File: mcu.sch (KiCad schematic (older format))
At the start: 29 parts, among them IC2 LM4040CYM3-2.5, P1 CONN_01X02, SW1 SW_PUSH, SW2 Rotary_Switch, T2 MMBT3904, U2 STM32F072CB, Y1 8kHz, Y2 ABS25-32.768KHZ-6-T

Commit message: Updated R/C/L symbols to IEC 60617 style
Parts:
- D6: renamed from IC2; symbol TEXAS_LM4041A12DBZ -> LM4040
- LED1, LED2: symbol LED-RESCUE-MPPT_Charger_20A -> LED
- renumbered SW2 to S1
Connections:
- wire segments 118 -> 116
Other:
- note added: "min. 65 uA\noperating\ncurrent"
- note removed: "L4: Murata\nBLM18AG601SN1D"
- note removed: "min. 65 uA operating\ncurrent needed"
- moved on the sheet: C27, C28, C29, C30, C31, C32, C33, C34, C36, L4, P1, R30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

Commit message: Updated revision: 0.8
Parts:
- removed C27, C28: 4.3p, Capacitors_SMD:C_0603, symbol C
- removed R30: 0, Resistors_SMD:R_0603, symbol R
- removed S1: Rotary_Switch, LibreSolar:Rotary_Switch_THT, symbol Rotary_Switch
- removed Y2: ABS25-32.768KHZ-6-T, Crystals:Crystal_SMD_SeikoEpson_MC306-4pin_8.0x3.2mm, symbol Crystal_NC23
- added C22: 100n, LibreSolar:C_0603_1608, symbol C
- added LED3, LED4: LED, LEDs:LED_0603, symbol LED
- added R31, R32: 2.2k, LibreSolar:R_0603_1608, symbol R
- added U6: 24AA01, TO_SOT_Packages_SMD:SOT-23-5, symbol 24AA01
- C29, C30, C31, C32, C34: footprint Capacitors_SMD:C_0603 -> LibreSolar:C_0603_1608; MFR Murata -> (none); MPN GRM188R71H104KA93D -> (none); Manufacturer (none) -> Murata; PartNumber (none) -> GRM188R71H104KA93D
- C33, C36: footprint Capacitors_SMD:C_0603 -> LibreSolar:C_0603_1608; MFR Murata -> (none); MPN GRM188R60J225KE19D -> (none); Manufacturer (none) -> Murata; PartNumber (none) -> GRM188R60J225KE19D
- D6: footprint TO_SOT_Packages_SMD:SOT-23 -> LibreSolar:SOT-23; MFR Microchip -> (none); MPN LM4040DYM3-2.5-TR -> (none); Manufacturer (none) -> Microchip; PartNumber (none) -> LM4040DYM3-2.5-TR
- L4: value L -> 600R; MFR Murata -> (none); MPN BLM18AG601SN1D -> (none); Manufacturer (none) -> Murata; PartNumber (none) -> BLM18AG601SN1D
- R37: footprint Resistors_SMD:R_0603 -> LibreSolar:R_0603_1608; MFR Yageo -> (none); MPN RC0603FR-07150KL -> (none); Manufacturer (none) -> Yageo; PartNumber (none) -> RC0603FR-07150KL
- R39, R40: footprint Resistors_SMD:R_0603 -> LibreSolar:R_0603_1608; MFR Yageo -> (none); MPN RC0603FR-071ML -> (none); Manufacturer (none) -> Yageo; PartNumber (none) -> RC0603FR-071ML
- R41: footprint Resistors_SMD:R_0603 -> LibreSolar:R_0603_1608; MFR Yageo -> (none); MPN RC0603FR-072K2L -> (none); Manufacturer (none) -> Yageo; PartNumber (none) -> RC0603FR-072K2L
- R42, R43: footprint Resistors_SMD:R_0603 -> LibreSolar:R_0603_1608; MFR Yageo -> (none); MPN RC0603FR-07330RL -> (none); Manufacturer (none) -> Yageo; PartNumber (none) -> RC0603FR-07330RL
- R45: footprint Resistors_SMD:R_0603 -> LibreSolar:R_0603_1608; MFR Yageo -> (none); MPN RC0603FR-0756KL -> (none); Manufacturer (none) -> Yageo; PartNumber (none) -> RC0603FR-0756KL
- SW1: footprint Buttons_Switches_THT:SW_PUSH_6mm -> LibreSolar:SW_SPST_EVQP7A; Manufacturer (none) -> C&K Components; PartNumber (none) -> PTS840 GK SMTR LFS
- T2: footprint TO_SOT_Packages_SMD:SOT-23 -> LibreSolar:SOT-23; MFR Diodes Inc. -> (none); MPN MMBT3904-7-F -> (none); Manufacturer (none) -> Diodes Inc.; PartNumber (none) -> MMBT3904-7-F
- U2: MFR STMicroelectronics -> (none); MPN STM32F072CB -> (none); Manufacturer (none) -> STMicroelectronics; PartNumber (none) -> STM32F072CBT6
- Y1: symbol CRYSTAL_SMD -> Resonator; MFR Murata -> (none); MPN CSTCE8M00G15C99-R0 -> (none); Manufacturer (none) -> Murata; PartNumber (none) -> CSTCE8M00G15C99-R0; Tolerance (none) -> 0.1%
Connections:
- net +3V3: now also C22.1, R31.2, R32.2, U6.4 (VCC)
- net GND: now also C22.2, LED3.1 (K), LED4.1 (K), U6.2 (GND), U6.5 (WP)
- net at LED1.2 (A), R42.1: now also LED3.2 (A)
- net at LED2.2 (A), R43.1: now also LED4.2 (A)
- net REF_I_DCDC renamed DAC
- net ROT_0 renamed I2C2_SCL
- net I2C2_SCL: now also R31.1, U6.1 (SCL)
- net ROT_1 renamed I2C2_SDA
- net I2C2_SDA: now also R32.1, U6.3 (SDA)
- net ROT_2 renamed 5V_OUT_EN
- no-connect marks 4 -> 3
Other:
- note added: "EEPROM"
- note added: "Equations:\ntau = R39 * C36 = 2.2 s\nV(t) = Vmax * (1-exp(-t/tau))\n--> t = -tau * ln(1-V/Vmax)\n\nNormal startup:\nBOOT0 < 0.69 V\nPress SW1 < 0.51 s\n\nUSB bootloader:\nBOOT0 > 1.61 V\nPress SW1 > 1.47 s"
- note added: "Tight tolerance\nfor CAN interface"
- note removed: "Mode switch"
- note removed: "Reset & boot switch\n- Press long (>2s) for USB bootloader\n (BOOT0 cap charged)\n- Press short (<1s) for normal reset"
- note removed: "Should be 0.1% tolerance\nfor CAN interface, e.g.\nCSTCE8M00G15C99-R0"
- moved on the sheet: C29, C30, C31, C32, C33, C36, D6, LED1, LED2, R37, R39, R40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

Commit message: Minor changes and gerber export update
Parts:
- C33, C36: Remarks (none) -> 6.3V, X5R
- Y1: Remarks (none) -> 0.1% tolerance; Tolerance 0.1% -> (none)
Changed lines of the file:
@@
 F 7 "" H 3600 -700 50  0001 C CNN "SPN"
 F 8 "" H 3600 -700 50  0001 C CNN "SPURL"
+F 9 "" H 0   0   60  0001 C CNN "Comment"
+F 10 "6.3V, X5R" H 0   0   60  0001 C CNN "Remarks"
 	1    6050 4800
 	1    0    0    -1
@@
 F 7 "" H -250 0   50  0001 C CNN "SPN"
 F 8 "" H -250 0   50  0001 C CNN "SPURL"
+F 9 "" H 0   0   60  0001 C CNN "Comment"
+F 10 "6.3V, X5R" H 0   0   60  0001 C CNN "Remarks"
 	1    9100 2700
 	1    0    0    -1
@@
 F 4 "Murata" H 0   -2950 50  0001 C CNN "Manufacturer"
 F 5 "CSTCE8M00G15C99-R0" H 0   -2950 50  0001 C CNN "PartNumber"
-F 6 "0.1%" H 5150 1150 50  0000 L CNN "Tolerance"
+F 6 "" H 5150 1150 50  0000 L CNN "Tolerance"
+F 7 "0.1% tolerance" H 0   0   60  0001 C CNN "Remarks"
 	1    5100 1400
 	1    0    0    -1

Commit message: V0.8.1: Small changes and update to new kicad symbol library table (nightlies only)
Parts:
- removed LED3, LED4: LED, LEDs:LED_0603, symbol LED
- C22, C29, C30, C31, C32, C33, C34, C36: symbol C -> device:C_Small
- D6: symbol LM4040 -> device:D_Zener_Small
- L4: symbol L -> device:L_Small
- LED1: footprint LEDs:LED_D3.0mm -> LEDs:LED_0603; symbol LED -> device:LED_Small; Manufacturer (none) -> Lite-On; PartNumber (none) -> LTST-C190KRKT; Remarks (none) -> red
- LED2: footprint LEDs:LED_D3.0mm -> LEDs:LED_0603; symbol LED -> device:LED_Small; Manufacturer (none) -> Lite-On; PartNumber (none) -> LTST-C190GKT
- P1: symbol CONN_01X02 -> Connector:Conn_01x02
- R31, R32, R37, R39, R40, R41, R42, R43, R45: symbol R -> device:R_Small
- SW1: symbol SW_PUSH -> IEC-60617:SW_PUSH
- SWD1: symbol ST_Nucleo_SWD -> LibreSolar:ST_Nucleo_SWD
- T2: symbol MMBT3904 -> Transistor:BC817
- U2: symbol STM32F072CB -> LibreSolar:STM32F072CB
- U6: symbol 24AA01 -> LibreSolar:24AA01; PartNumber 24AA01 -> 24AA32AFT-I/OT
- Y1: value 8kHz -> 8MHz; footprint LibreSolar:Resonator_Murata_CSTCE -> LibreSolar:Resonator_Murata_CSTCE_G; symbol Resonator -> device:Resonator_Small; Tolerance (none) -> 0.1%
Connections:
- net GND: now also Y1.2; no longer Y1.3
- net OSC_OUT: now also Y1.3; no longer Y1.2
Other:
- moved on the sheet: LED1, LED2, R42, R43

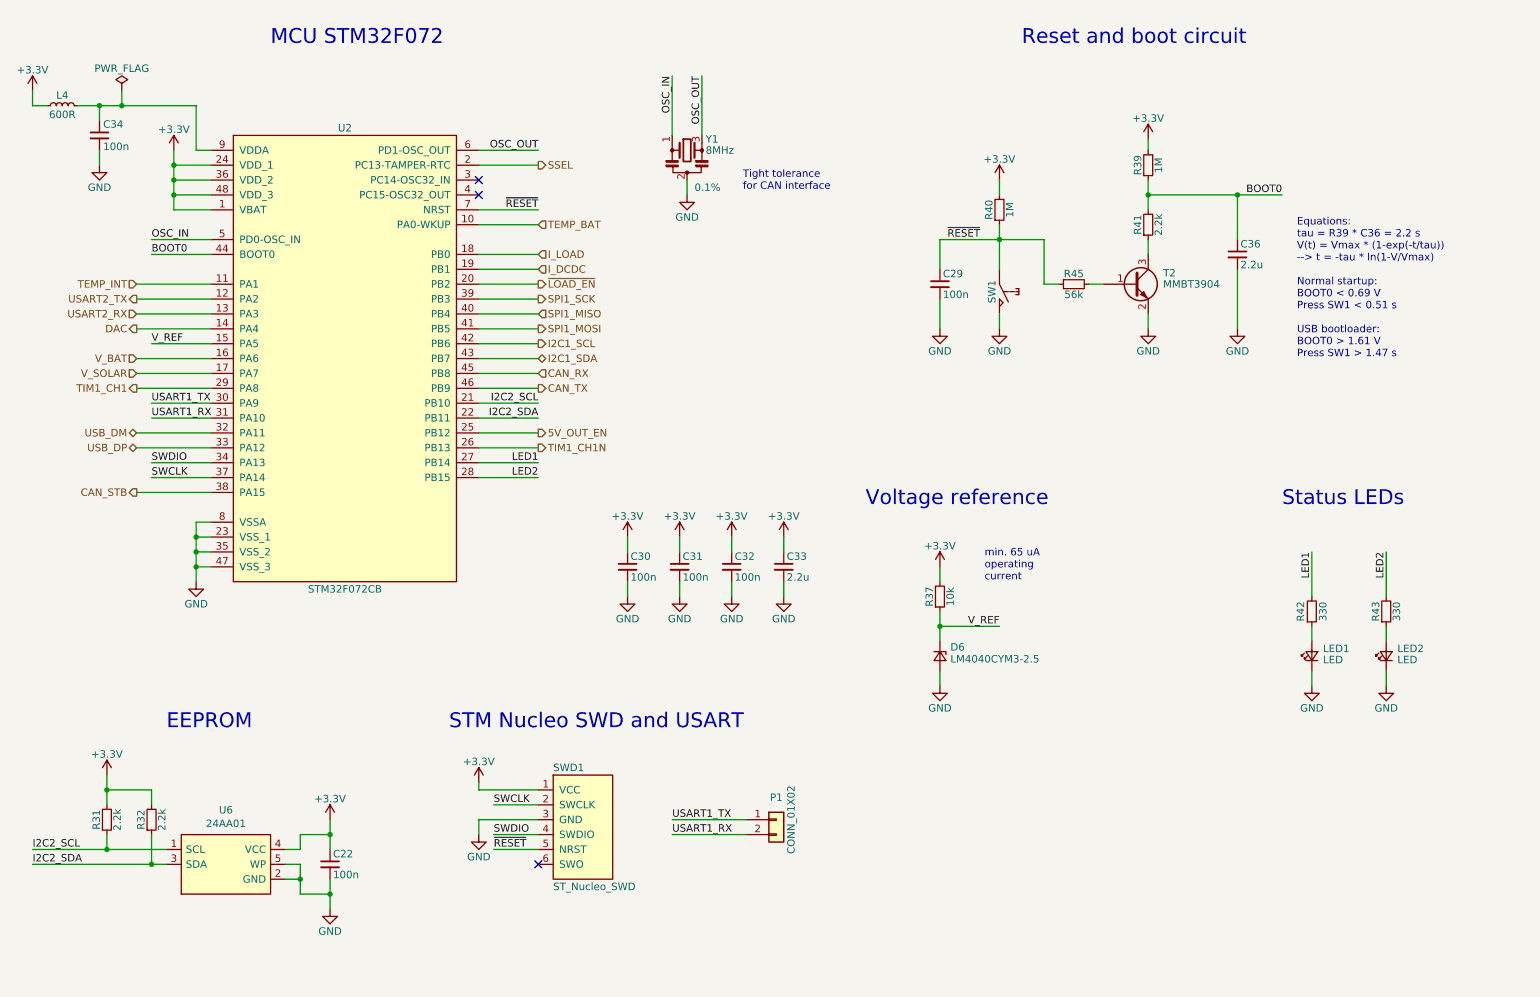
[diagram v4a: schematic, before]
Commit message: Revision 0.9 for first small production batch - Switchable power supply for bus and UEXT (to be make sure to reach very low power consumption during LVD conditions) - MLCCs for EMC added to each high power input/output - Re-arrangement of some connectors after initial tests with housing
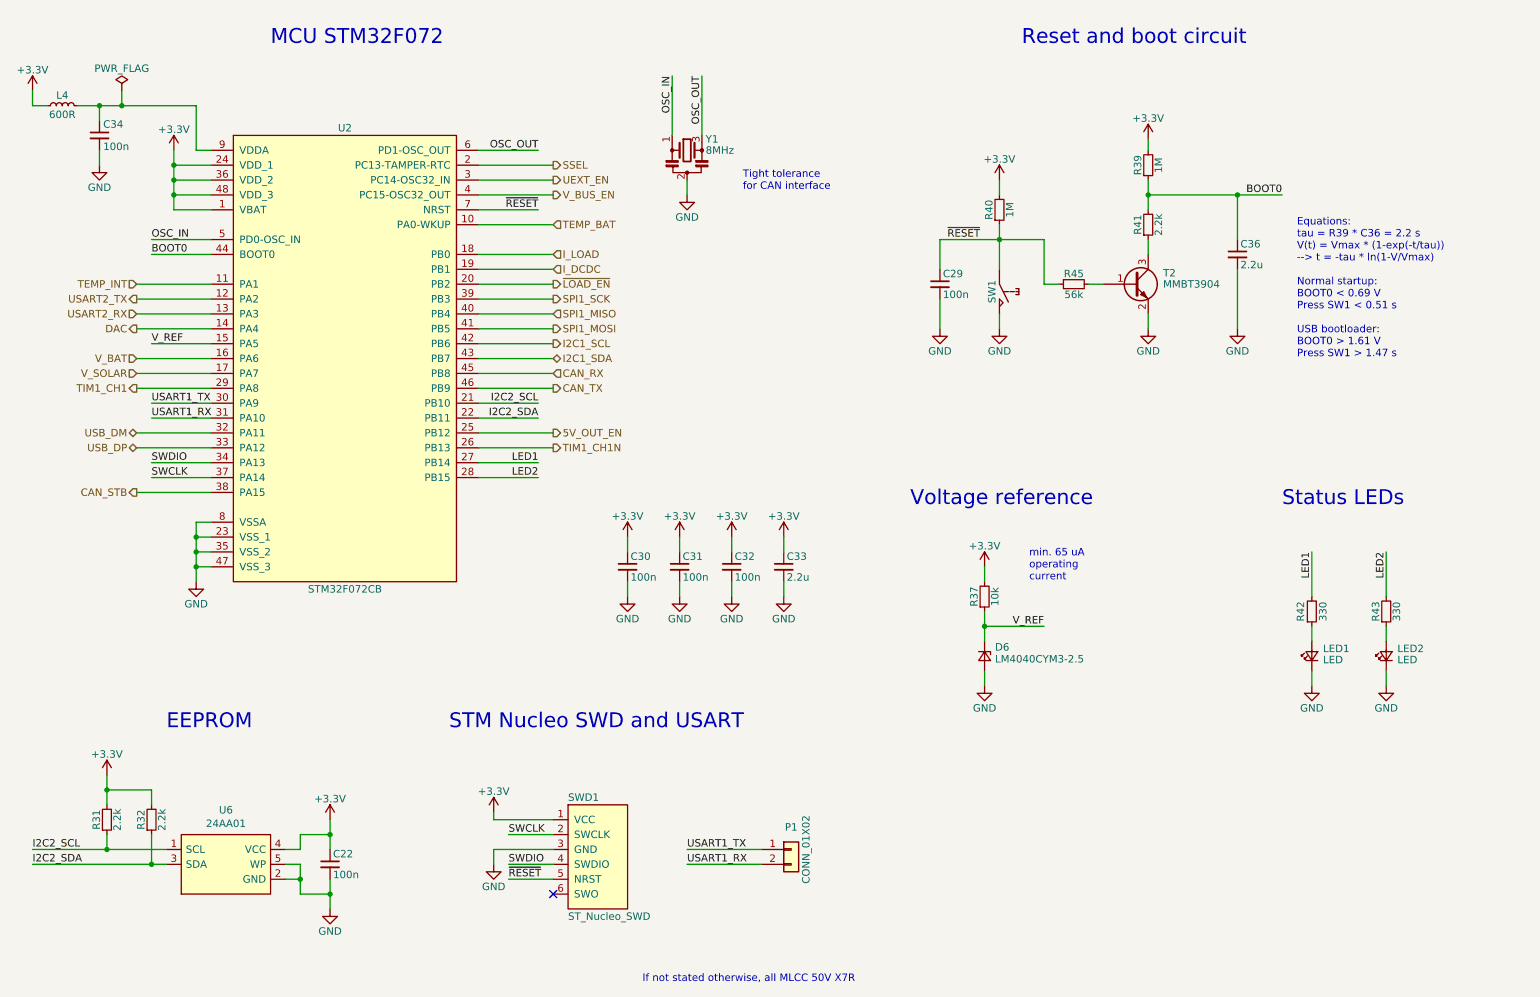
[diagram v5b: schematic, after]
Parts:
- R37: PartNumber RC0603FR-07150KL -> RC0603FR-0710KL
- Y1: Tolerance 0.1% -> (none)
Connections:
- net UEXT_EN: now reaches U2.3 (PC14-OSC32_IN)
- net V_BUS_EN: now reaches U2.4 (PC15-OSC32_OUT)
- no-connect marks 3 -> 1
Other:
- note added: "If not stated otherwise, all MLCC 50V X7R"
- moved on the sheet: D6, P1, R37, SWD1

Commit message: BOM updated
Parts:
- LED1: value LED -> LED_red
- LED2: value LED -> LED_green
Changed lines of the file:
@@
 AR Path="/58A68DCB/58AE11BD" Ref="LED2"  Part="1"
 F 0 "LED2" V 10150 5325 50  0000 R CNN
-F 1 "LED" V 10075 5325 50  0000 R CNN
+F 1 "LED_green" V 10075 5325 50  0000 R CNN
 F 2 "LEDs:LED_0603" V 10100 5400 50  0001 C CNN
 F 3 "" V 10100 5400 50  0001 C CNN
@@
 AR Path="/58A68DCB/58AE0EA3" Ref="LED1"  Part="1"
 F 0 "LED1" V 9650 5325 50  0000 R CNN
-F 1 "LED" V 9575 5325 50  0000 R CNN
+F 1 "LED_red" V 9575 5325 50  0000 R CNN
 F 2 "LEDs:LED_0603" V 9600 5400 50  0001 C CNN
 F 3 "" V 9600 5400 50  0001 C CNN

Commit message: Final version for Jan/2018 production
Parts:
- C33, C36: PartNumber GRM188R60J225KE19D -> GRM188R61E225KA12D; Remarks 6.3V, X5R -> 25V, X5R
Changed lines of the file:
@@
 Sheet 3 6
 Title "MPPT Charger 20A"
-Date "2017-12-11"
-Rev "0.9"
+Date "2018-01-18"
+Rev "0.10"
 Comp "Libre Solar"
 Comment1 "Author: Martin Jäger"
@@
 F 3 "" H 6050 4800 50  0000 C CNN
 F 4 "Murata" H 3600 -700 50  0001 C CNN "Manufacturer"
-F 5 "GRM188R60J225KE19D" H 3600 -700 50  0001 C CNN "PartNumber"
-F 6 "6.3V, X5R" H 0   0   60  0001 C CNN "Remarks"
+F 5 "GRM188R61E225KA12D" H 3600 -700 50  0001 C CNN "PartNumber"
+F 6 "25V, X5R" H 0   0   60  0001 C CNN "Remarks"
 	1    6050 4800
 	1    0    0    -1
@@
 F 3 "" H 9100 2700 50  0000 C CNN
 F 4 "Murata" H -250 0   50  0001 C CNN "Manufacturer"
-F 5 "GRM188R60J225KE19D" H -250 0   50  0001 C CNN "PartNumber"
-F 6 "6.3V, X5R" H 0   0   60  0001 C CNN "Remarks"
+F 5 "GRM188R61E225KA12D" H -250 0   50  0001 C CNN "PartNumber"
+F 6 "25V, X5R" H 0   0   60  0001 C CNN "Remarks"
 	1    9100 2700
 	1    0    0    -1
